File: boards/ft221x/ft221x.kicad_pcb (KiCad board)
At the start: 2 copper layers, 17.8 x 26.7 mm, 12 parts, among them J1 USB_B_Micro, J2 BREADBOARD_A, J3 BREADBOARD_B, J4 BREAKOUT_SPI1, U1 FT221XS

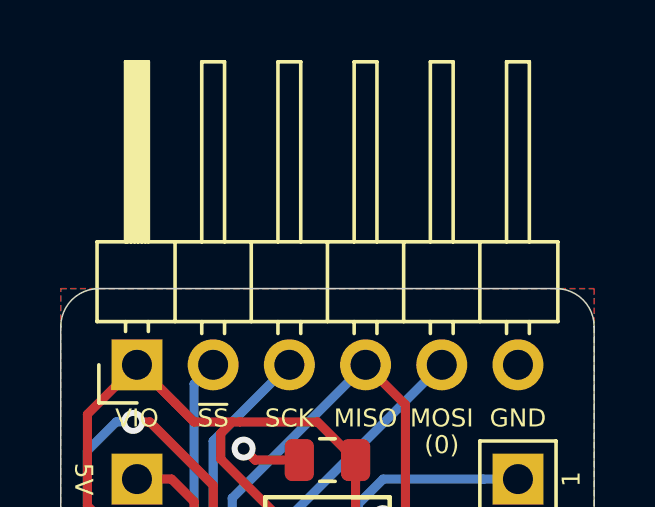
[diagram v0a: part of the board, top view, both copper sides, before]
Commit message: Updated soldermask clearance, DRC rules, gerbers, and BOMs.
* ft221
* atsamd21e18a
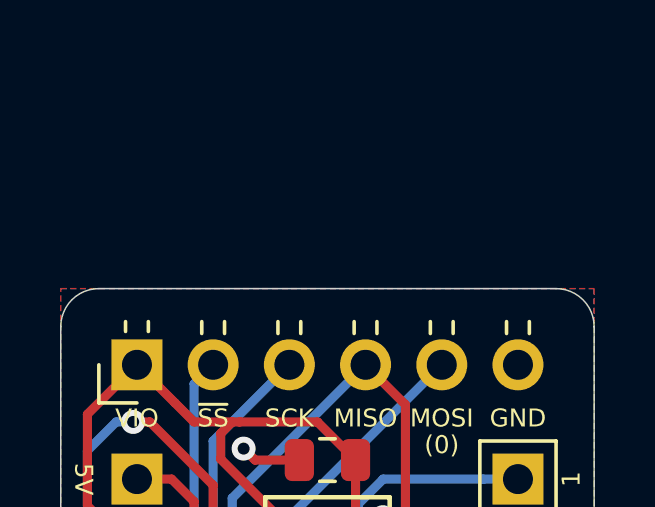
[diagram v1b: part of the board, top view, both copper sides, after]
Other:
- rule trace_min: 0.1016 -> 0.09
- rule via_min_drill: 0.3 -> 0.2
- rule via_min_size: 0.1016 -> 0.45
